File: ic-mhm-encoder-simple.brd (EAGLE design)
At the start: 68 x 58.3 mm, 35 parts, among them IC1 LS7183-SOIC, J1 2023960907, J2 2023960607, M1 BSS670S2LH6327XTSA1, SW1 CS-4-13NTA, U1 24LC16BT-I/MC, U2 1SS308(TE85L,F, U3 1SS308(TE85L,F, U4 1SS308(TE85L,F

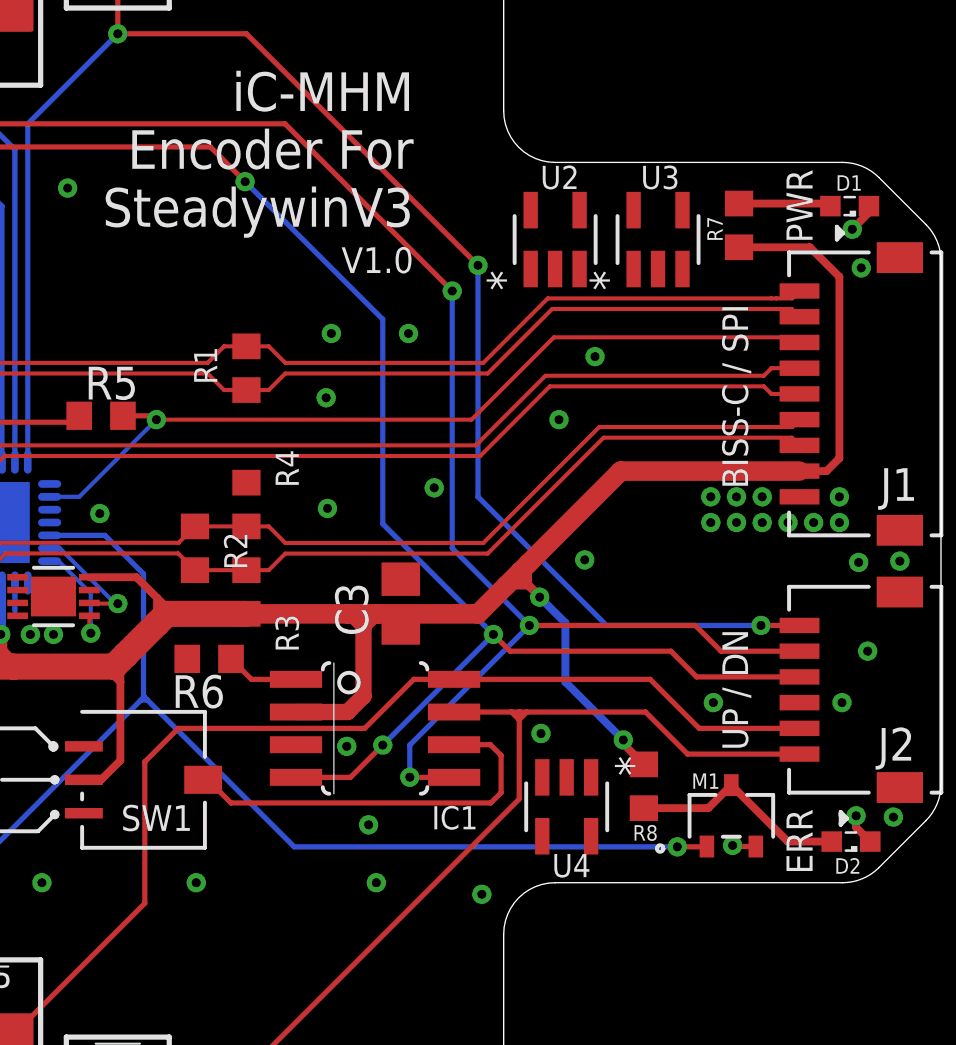
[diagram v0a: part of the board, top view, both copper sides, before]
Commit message: Routed ESD Diodes
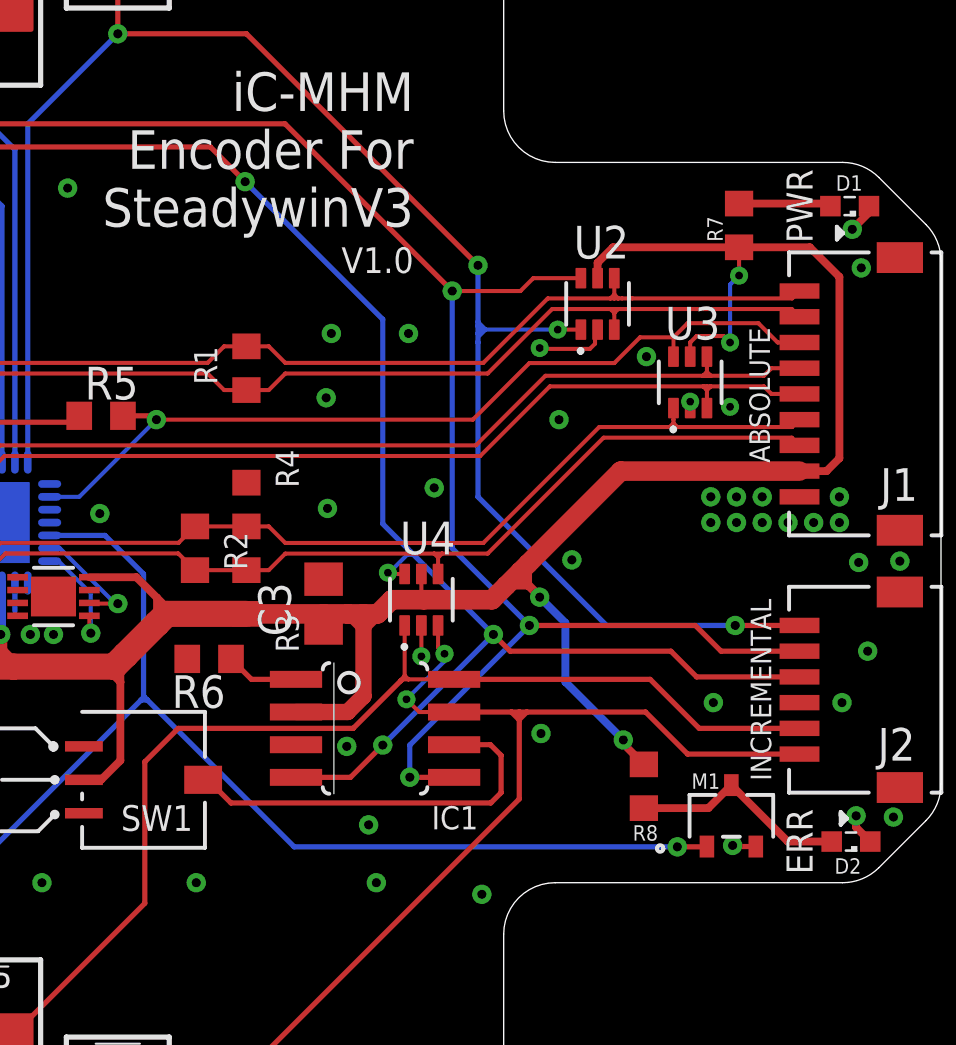
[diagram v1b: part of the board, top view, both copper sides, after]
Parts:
- U2, U3, U4: value 1SS308(TE85L,F -> D5V0F4U6S-7; device ic-mhm:SOT-25___(SMV)_TOS -> ic-mhm:SOT-363_DIO
- moved U4 9.83 mm to (16.8, -3.00), turned to 90 degrees
- moved U3 5.69 mm to (27.2, 5.45)
- moved C3 3.00 mm to (13.0, -3.15)
- moved U2 3.00 mm to (23.6, 8.50)
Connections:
- net !DN: now also U4.3
- net !UP: now also U4.1
- net ENC_A: now also U4.6
- net ENC_B: now also U2.6
- net ENC_Z: now also U2.1
- net GND: now also U2.2, U3.2, U4.2
- net MA_N: now also U2.3
- net MA_P: now also U2.4
- net NCS: now also U3.6
- net SLI_N: now also U4.4
- net SLI_P: now also U3.1
- net SLO_N: now also U3.3
- net SLO_P: now also U3.4
- net VDD: now also U2.5, U3.5, U4.5
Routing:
- net VDD: track 126.3 -> 140.4 mm, vias 6 -> 8
- net !DN: track 39.0 -> 44.7 mm, vias 0 -> 2
- net ENC_Z: track 63.4 -> 68.7 mm, vias 3 -> 4
- net ENC_B: track 73.5 -> 78.7 mm
- net GND: track 9.81 -> 14.0 mm, vias 62 -> 66
- net !UP: track 41.3 -> 43.7 mm
- net ENC_A: track 73.9 -> 76.2 mm, vias 4 -> 5
- net SLO_N: track 39.8 -> 41.0 mm
- net MA_N: track 37.7 -> 39.0 mm
- net MA_P: track 38.6 -> 39.8 mm
- net NCS: track 33.2 -> 34.4 mm
- net SLO_P: track 40.0 -> 41.1 mm
- net SLI_P: track 38.4 -> 39.5 mm
- net SLI_N: track 37.9 -> 39.0 mm
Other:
- board text added: "ABSOLUTE"
- board text added: "INCREMENTAL"
- board text removed: "BISS-C / SPI"
- board text removed: "UP / DN"

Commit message: changed RBIAS and added note about range
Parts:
- R6: value 715K -> 649K
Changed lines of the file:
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@@
 </layers>
 <board>
-<fusionsync huburn="a.cGVyc29uYWw6dWUyZDc2YTg0" projecturn="a.cGVyc29uYWw6dWUyZDc2YTg0I0QyMDE4MTAxMTE1NDA5NDkwMQ" f3durn="urn:adsk.wipprod:dm.lineage:cRy2wqOgSwGWjgXRfm9aog" pcbguid="" lastpulledtime="" lastsyncedchangeguid="" latestrevisionid="3380200f-ce55-481d-b55a-b27747c47f31" lastsyncedrevisionid="3380200f-ce55-481d-b55a-b27747c47f31" lastboardhashguid="841a098c-36e2-2afa-04b2-54153f3a2ca9" lastpushedtime="2021-11-24T07:05:37Z" linktopcb3d="true"/>
+<fusionsync huburn="a.cGVyc29uYWw6dWUyZDc2YTg0" projecturn="a.cGVyc29uYWw6dWUyZDc2YTg0I0QyMDE4MTAxMTE1NDA5NDkwMQ" f3durn="urn:adsk.wipprod:dm.lineage:cRy2wqOgSwGWjgXRfm9aog" pcbguid="" lastpulledtime="" lastsyncedchangeguid="" latestrevisionid="bf94aacb-a219-4fe9-a260-961f2c0cfe42" lastsyncedrevisionid="bf94aacb-a219-4fe9-a260-961f2c0cfe42" lastboardhashguid="8f8cbafc-e03e-f323-aa5e-8949940b47b4" lastpushedtime="2021-11-29T05:07:52Z" linktopcb3d="true"/>
 <plain>
 <wire x1="10.00001875" y1="28.867509375" x2="-29.99998125" y2="5.7735" width="0" layer="20"/>
@@
 <attribute name="VALUE" x="15.54" y="-4.42" size="1.27" layer="27" rot="R90"/>
 </element>
-<element name="R6" library="rcl" library_urn="urn:adsk.eagle:library:334" package="R0603" package3d_urn="urn:adsk.eagle:package:23555/3" value="715K" x="8.55" y="-5.3" smashed="yes" rot="R180">
+<element name="R6" library="rcl" library_urn="urn:adsk.eagle:library:334" package="R0603" package3d_urn="urn:adsk.eagle:package:23555/3" value="649K" x="8.55" y="-5.3" smashed="yes" rot="R180">
 <attribute name="NAME" x="9.185" y="-5.935" size="1.27" layer="25" rot="R180"/>
 <attribute name="POPULARITY" value="77" x="8.55" y="-5.3" size="2" layer="27" font="vector" rot="R180" display="off"/>

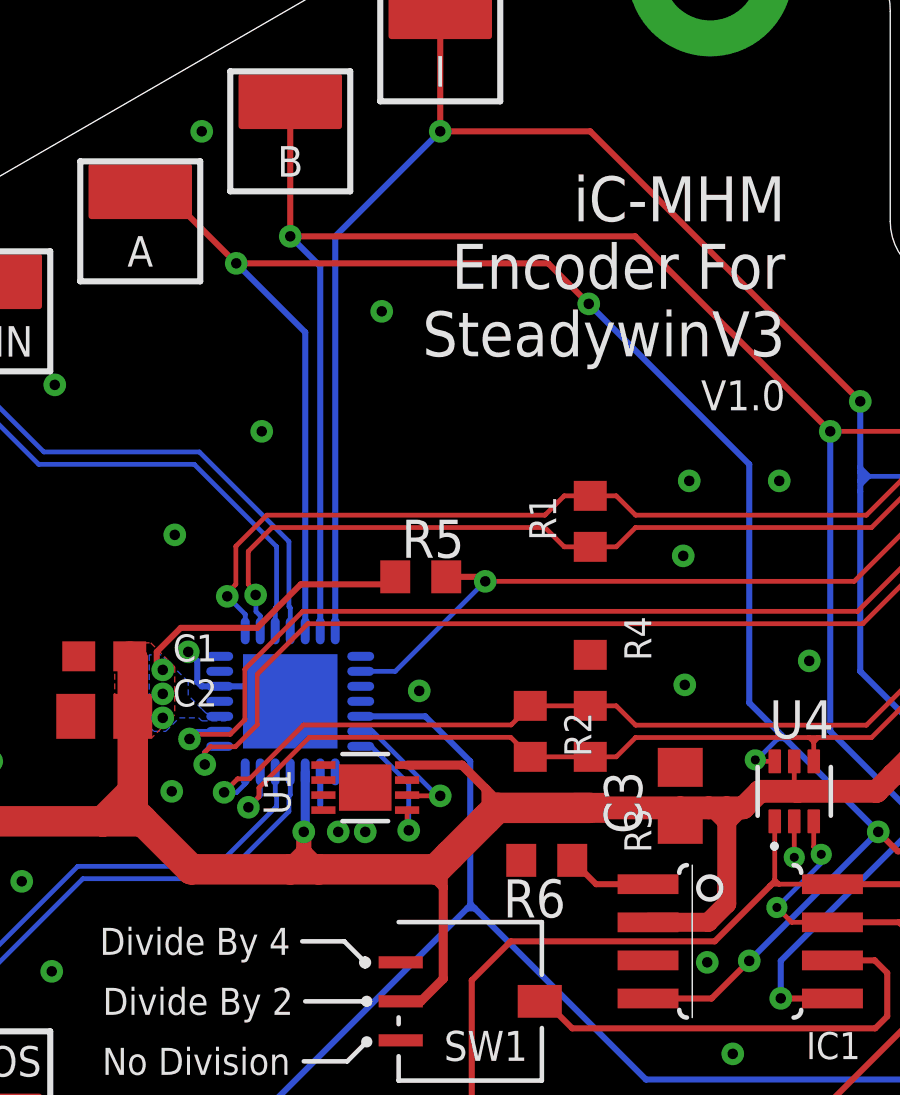
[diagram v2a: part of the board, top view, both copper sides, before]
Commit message: Improved GND vias
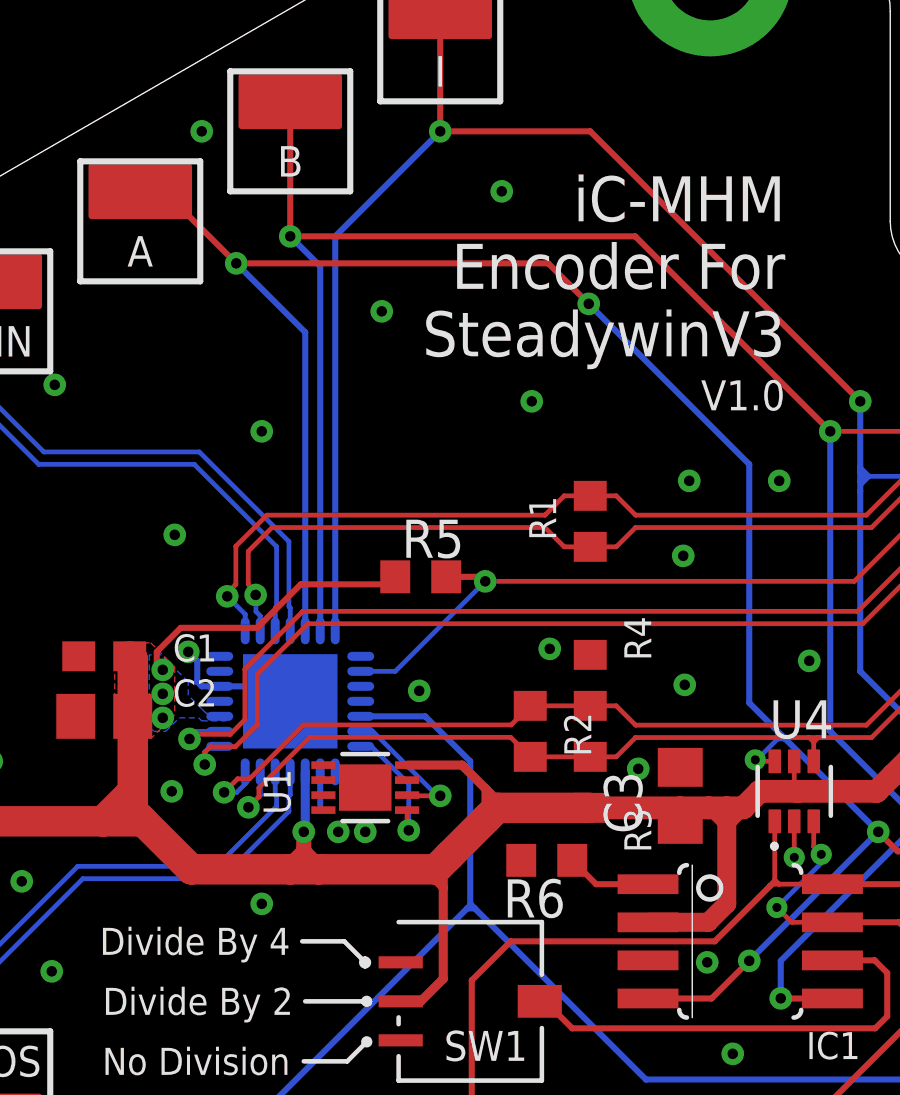
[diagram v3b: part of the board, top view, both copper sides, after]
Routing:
- net GND: vias 66 -> 71
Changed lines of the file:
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@@
 <wire x1="21.434975" y1="6.75" x2="21.4" y2="6.784975" width="0.15875" layer="1"/>
 <via x="21.4" y="6.784975" extent="1-16" drill="0.3"/>
+<via x="7.05" y="17" extent="1-16" drill="0.35"/>
+<via x="8.05" y="10" extent="1-16" drill="0.35"/>
+<via x="8.65" y="1.75" extent="1-16" drill="0.35"/>
+<via x="11.6" y="-2.25" extent="1-16" drill="0.35"/>
+<via x="-0.95" y="-6.75" extent="1-16" drill="0.35"/>
 <wire x1="33.9" y1="9.9" x2="35.4" y2="10.3" width="0" layer="19" extent="1-1"/>
 <wire x1="33.55" y1="11.4" x2="33.9" y2="9.9" width="0" layer="19" extent="1-1"/>
 <wire x1="28.8" y1="4.5" x2="33.9" y2="9.9" width="0" layer="19" extent="1-1"/>
-<wire x1="27.25" y1="4.7" x2="28.8" y2="4.5" width="0" layer="19" extent="1-1"/>
-<wire x1="27.25" y1="4.45" x2="27.25" y2="4.7" width="0" layer="19" extent="1-1"/>
+<wire x1="27.25" y1="4.45" x2="28.8" y2="4.5" width="0" layer="19" extent="1-1"/>
+<wire x1="27.25" y1="4.7" x2="27.25" y2="4.45" width="0" layer="19" extent="1-1"/>
 <wire x1="25.55" y1="6.45" x2="27.25" y2="4.7" width="0" layer="19" extent="1-1"/>
-<wire x1="23.55" y1="7.4" x2="25.55" y2="6.45" width="0" layer="19" extent="1-1"/>
+<wire x1="23.65" y1="7.5" x2="25.55" y2="6.45" width="0" layer="19" extent="1-1"/>
 <wire x1="22.15" y1="4" x2="21.4" y2="6.784975" width="0" layer="19" extent="1-1"/>
-<wire x1="30.05" y1="1" x2="28.8" y2="4.5" width="0" layer="19" extent="1-1"/>
+<wire x1="29.05" y1="1" x2="28.8" y2="4.5" width="0" layer="19" extent="1-1"/>
+<wire x1="30.05" y1="1" x2="29.05" y2="1" width="0" layer="19" extent="1-1"/>
 <wire x1="30.05" y1="0" x2="30.05" y2="1" width="0" layer="19" extent="1-1"/>
 <wire x1="31.05" y1="0" x2="30.05" y2="0" width="0" layer="19" extent="1-1"/>
@@
 <wire x1="33.05" y1="0" x2="32.05" y2="0" width="0" layer="19" extent="1-1"/>
 <wire x1="33.05" y1="1" x2="33.05" y2="0" width="0" layer="19" extent="1-1"/>
-<wire x1="29.05" y1="1" x2="30.05" y2="1" width="0" layer="19" extent="1-1"/>
-<wire x1="29.05" y1="0" x2="30.05" y2="0" width="0" layer="19" extent="1-1"/>
+<wire x1="29.05" y1="0" x2="29.05" y2="1" width="0" layer="19" extent="1-1"/>
 <wire x1="28.05" y1="0" x2="29.05" y2="0" width="0" layer="19" extent="1-1"/>
 <wire x1="28.05" y1="1" x2="29.05" y2="1" width="0" layer="19" extent="1-1"/>
@@
 <wire x1="13.15" y1="0.55" x2="13.1" y2="4.85" width="0" layer="19" extent="1-1"/>
 <wire x1="13" y1="-2.2" x2="13.15" y2="0.55" width="0" layer="19" extent="1-1"/>
+<wire x1="11.6" y1="-2.25" x2="13" y2="-2.2" width="0" layer="19" extent="1-1"/>
 <wire x1="10" y1="1.55" x2="13.15" y2="0.55" width="0" layer="19" extent="1-1"/>
+<wire x1="8.65" y1="1.75" x2="10" y2="1.55" width="0" layer="19" extent="1-1"/>
 <wire x1="16.8" y1="-4" x2="13" y2="-2.2" width="0" layer="19" extent="1-1"/>
 <wire x1="17.3" y1="1.35" x2="13.15" y2="0.55" width="0" layer="19" extent="1-1"/>
@@
 <wire x1="15.05" y1="-14" x2="14.75" y2="-11.75" width="0" layer="19" extent="1-1"/>
 <wire x1="19.15" y1="-14.45" x2="15.05" y2="-14" width="0" layer="19" extent="1-1"/>
-<wire x1="7.7" y1="-5.3" x2="11.9266" y2="-8.635" width="0" layer="19" extent="1-1"/>
-<wire x1="3.8946" y1="-2.6248" x2="7.7" y2="-5.3" width="0" layer="19" extent="1-1"/>
+<wire x1="4.3" y1="0.35" x2="8.65" y2="1.75" width="0" layer="19" extent="1-1"/>
+<wire x1="3.8946" y1="-2.6248" x2="4.3" y2="0.35" width="0" layer="19" extent="1-1"/>
 <wire x1="2.5" y1="-2.8748" x2="3.8946" y2="-2.6248" width="0" layer="19" extent="1-1"/>
 <wire x1="1.1054" y1="-2.6248" x2="2.5" y2="-2.8748" width="0" layer="19" extent="1-1"/>
@@
 <wire x1="1" y1="-1" x2="1.1054" y2="-2.1248" width="0" layer="19" extent="1-16"/>
 <wire x1="-0.35" y1="0.6" x2="0" y2="0" width="0" layer="19" extent="16-16"/>
-<wire x1="4.3" y1="0.35" x2="3.8946" y2="-2.6248" width="0" layer="19" extent="1-1"/>
+<wire x1="-0.95" y1="-6.75" x2="1.6" y2="-4.35" width="0" layer="19" extent="1-1"/>
 <wire x1="-7.05" y1="1.5" x2="-3.4" y2="1.65" width="0" layer="19" extent="1-1"/>
 <wire x1="-7.15" y1="-0.5" x2="-7.05" y2="1.5" width="0" layer="19" extent="1-1"/>
@@
 <wire x1="-0.95" y1="9" x2="-3.85" y2="5.55" width="0" layer="19" extent="1-1"/>
 <wire x1="3.6826" y1="-8.7" x2="2.5" y2="-4.35" width="0" layer="19" extent="1-1"/>
+<wire x1="7.7" y1="-5.3" x2="3.8946" y2="-2.6248" width="0" layer="19" extent="1-1"/>
 <wire x1="22.65" y1="-1.45" x2="22.15" y2="4" width="0" layer="19" extent="1-1"/>
 <wire x1="2.05" y1="-14" x2="3.6826" y2="-8.7" width="0" layer="19" extent="1-1"/>
 <wire x1="21.45" y1="-8.2" x2="16.8" y2="-5.2" width="0" layer="19" extent="1-1"/>
 <wire x1="3.05" y1="13" x2="-0.95" y2="9" width="0" layer="19" extent="1-1"/>
+<wire x1="7.05" y1="17" x2="3.05" y2="13" width="0" layer="19" extent="1-1"/>
+<wire x1="8.05" y1="10" x2="3.05" y2="13" width="0" layer="19" extent="1-1"/>
 <wire x1="-14.95" y1="-6" x2="-8.95" y2="-6" width="0" layer="19" extent="1-1"/>
 <wire x1="-19.95" y1="-6" x2="-14.95" y2="-6" width="0" layer="19" extent="1-1"/>

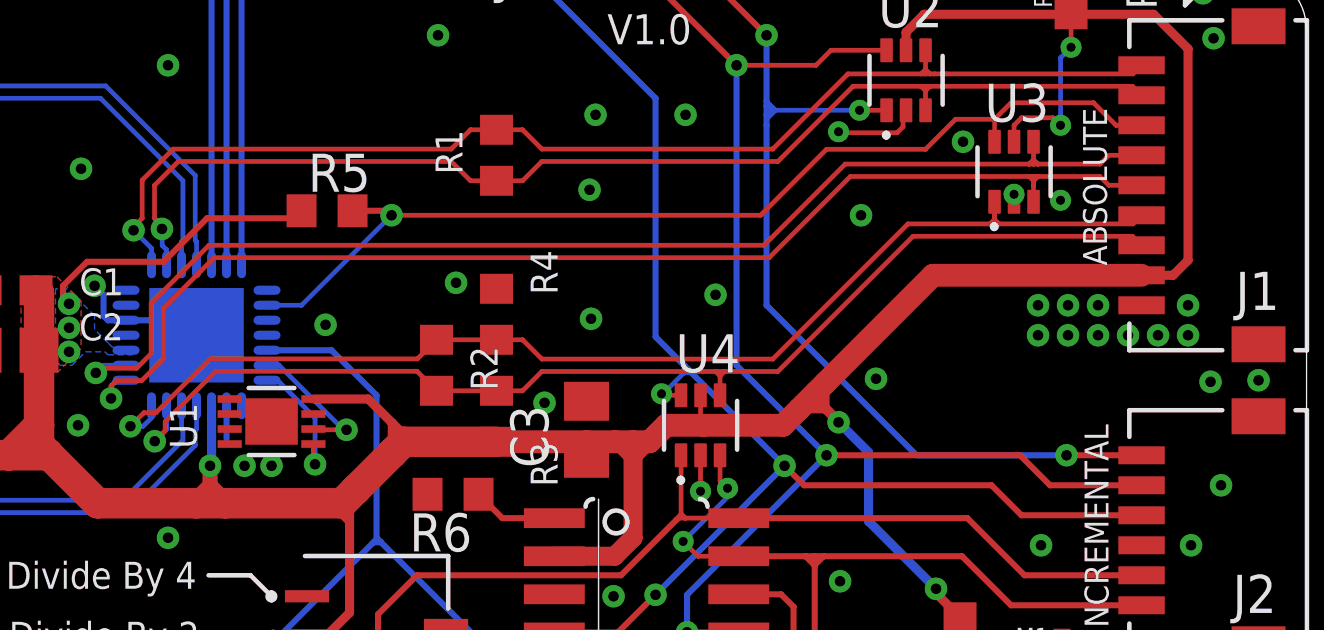
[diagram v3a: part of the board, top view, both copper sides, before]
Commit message: Fixed/Approved all DRC Errors
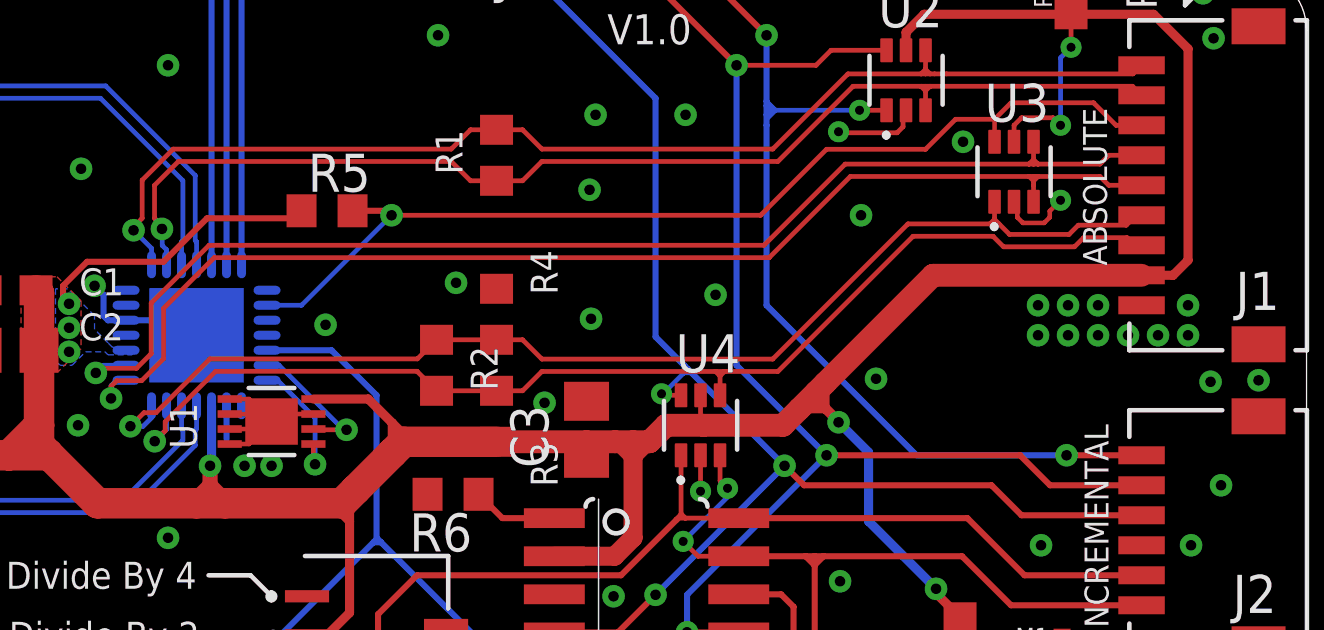
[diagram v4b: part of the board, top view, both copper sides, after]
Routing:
- net GND: track 14.0 -> 23.6 mm, vias 71 -> 70
